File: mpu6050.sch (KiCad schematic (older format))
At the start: 5 parts, among them U2 MPU6050

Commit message: added lots of stuff
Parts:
- added C29: 4.7u, Capacitors_SMD:C_0603, symbol C
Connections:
- net GND: now also C29.2
- net VCC: no longer C16.1, U2.13 (VDD)
- new net VCC_SEN: C16.1, C29.1, U2.13 (VDD)
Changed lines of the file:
@@
 EESchema Schematic File Version 2
+LIBS:stm32f4_lqfp64_mpu6050-rescue
 LIBS:power
 LIBS:device
@@
 LIBS:minimal
 LIBS:alis_parts
+LIBS:sensors
+LIBS:stm32
 LIBS:stm32f4_lqfp64_mpu6050-cache
 EELAYER 25 0
@@
 $Descr A4 11693 8268
 encoding utf-8
-Sheet 5 7
+Sheet 5 10
 Title ""
 Date ""
@@
 	5050 3650 5050 4450
 Wire Wire Line
-	5250 2500 5250 4150
-Wire Wire Line
 	5800 4050 4900 4050
 Wire Wire Line
@@
 	4700 3450 4700 4450
 Connection ~ 5250 4450
-Connection ~ 5250 3750
 Connection ~ 5450 4450
 Wire Wire Line
-	4700 4450 5450 4450
-Connection ~ 5250 3150
+	4400 4450 5450 4450
 Wire Wire Line
 	4700 3150 5800 3150
 Wire Wire Line
-	5800 3750 5250 3750
+	4400 3750 5800 3750
 Connection ~ 5450 3850
-Wire Wire Line
-	5800 3850 5450 3850
 Wire Wire Line
 	5450 2750 5450 4500
@@
 $EndComp
 $Comp
-L GND #PWR22
+L GND #PWR30
 U 1 1 569B8F29
 P 5450 4500
-F 0 "#PWR22" H 5450 4250 50  0001 C CNN
+F 0 "#PWR30" H 5450 4250 50  0001 C CNN
 F 1 "GND" H 5458 4326 50  0000 C CNN
 F 2 "" H 5450 4500 50  0000 C CNN
@@
 	1    0    0    -1
 $EndComp
-Text GLabel 5250 2500 0    60   Input ~ 0
+Text GLabel 4700 3150 0    60   Input ~ 0
 VCC
 Text GLabel 5800 4150 0    60   Input ~ 0
@@
 	1    0    0    -1
 $EndComp
+$Comp
+L C C29
+U 1 1 569B8FE4
+P 4400 4000
+F 0 "C29" H 4515 4046 50  0000 L CNN
+F 1 "4.7u" H 4515 3954 50  0000 L CNN
+F 2 "Capacitors_SMD:C_0603" H 4438 3850 50  0001 C CNN
+F 3 "" H 4400 4000 50  0000 C CNN
+	1    4400 4000
+	1    0    0    -1
+$EndComp
+Wire Wire Line
+	4400 4150 4400 4450
+Connection ~ 4700 4450
+Wire Wire Line
+	5800 3850 5450 3850
+Wire Wire Line
+	4400 3750 4400 3850
+Text GLabel 4400 3750 0    60   Input ~ 0
+VCC_SEN
+Wire Wire Line
+	5250 4150 5250 3750
+Connection ~ 5250 3750
 $EndSCHEMATC

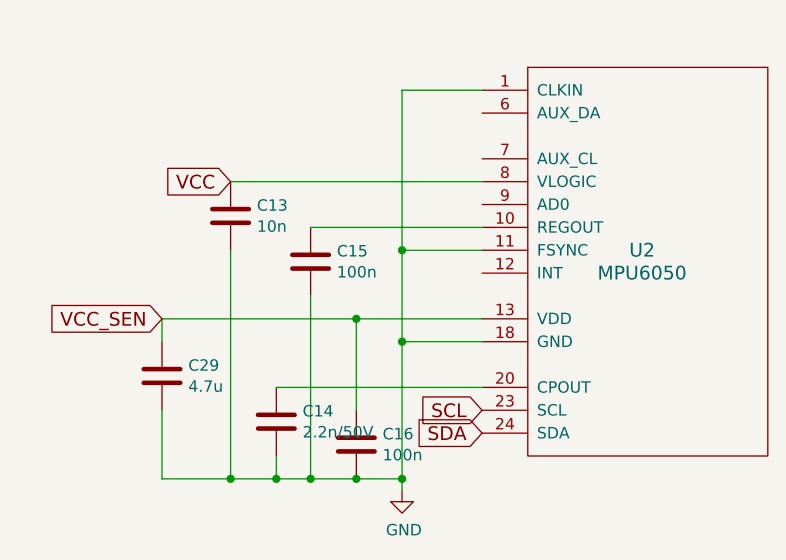
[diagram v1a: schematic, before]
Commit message: added IMU int and USB sense in schematic
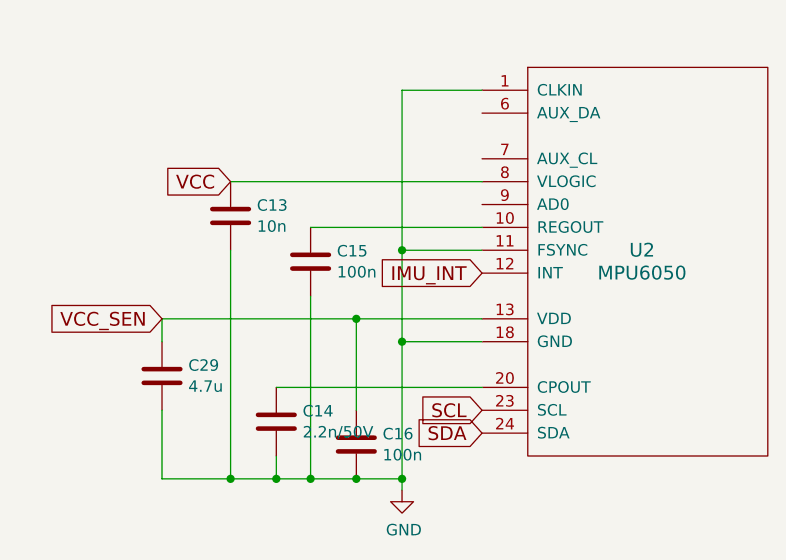
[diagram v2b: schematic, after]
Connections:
- net IMU_INT: now reaches U2.12 (INT)
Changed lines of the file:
@@
 	5250 4150 5250 3750
 Connection ~ 5250 3750
+Text GLabel 5800 3550 0    60   Input ~ 0
+IMU_INT
 $EndSCHEMATC

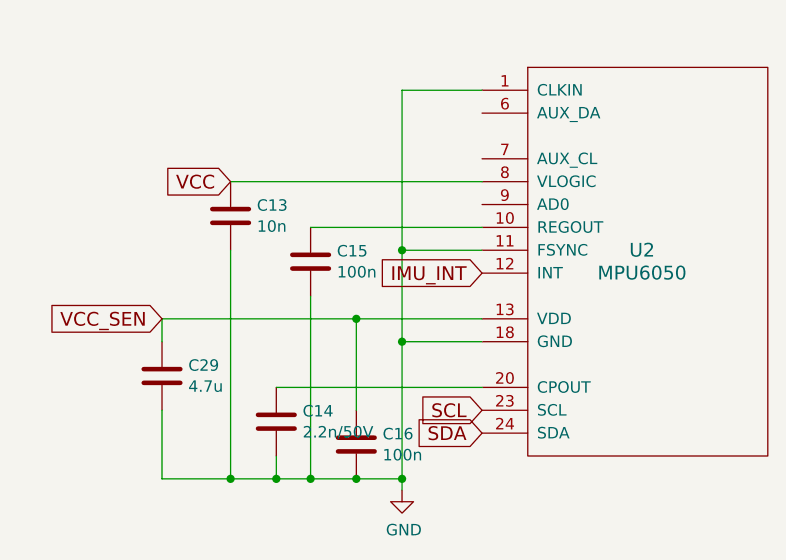
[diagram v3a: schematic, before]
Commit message: changed some netnames
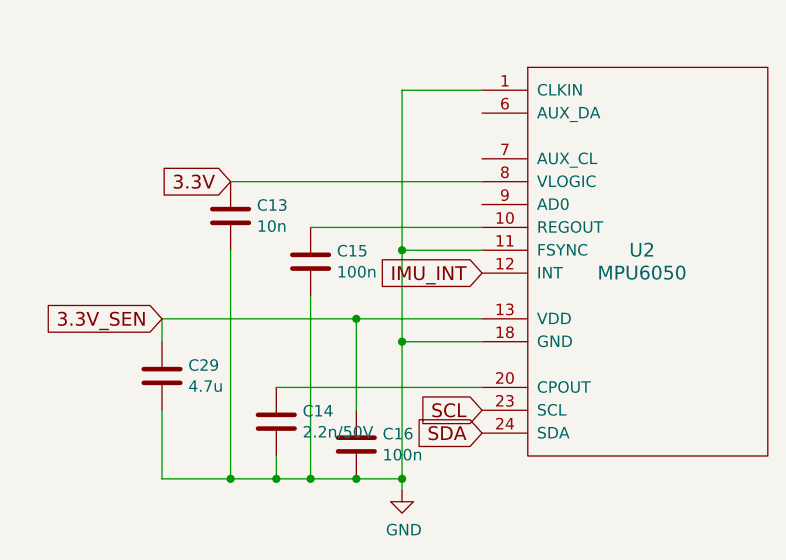
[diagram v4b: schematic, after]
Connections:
- net VCC renamed 3.3V
- net VCC_SEN renamed 3.3V_SEN
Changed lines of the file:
@@
 $EndComp
 $Comp
-L GND #PWR30
+L GND #PWR024
 U 1 1 569B8F29
 P 5450 4500
-F 0 "#PWR30" H 5450 4250 50  0001 C CNN
+F 0 "#PWR024" H 5450 4250 50  0001 C CNN
 F 1 "GND" H 5458 4326 50  0000 C CNN
 F 2 "" H 5450 4500 50  0000 C CNN
@@
 $EndComp
 Text GLabel 4700 3150 0    60   Input ~ 0
-VCC
+3.3V
 Text GLabel 5800 4150 0    60   Input ~ 0
 SCL
@@
 	4400 3750 4400 3850
 Text GLabel 4400 3750 0    60   Input ~ 0
-VCC_SEN
+3.3V_SEN
 Wire Wire Line
 	5250 4150 5250 3750

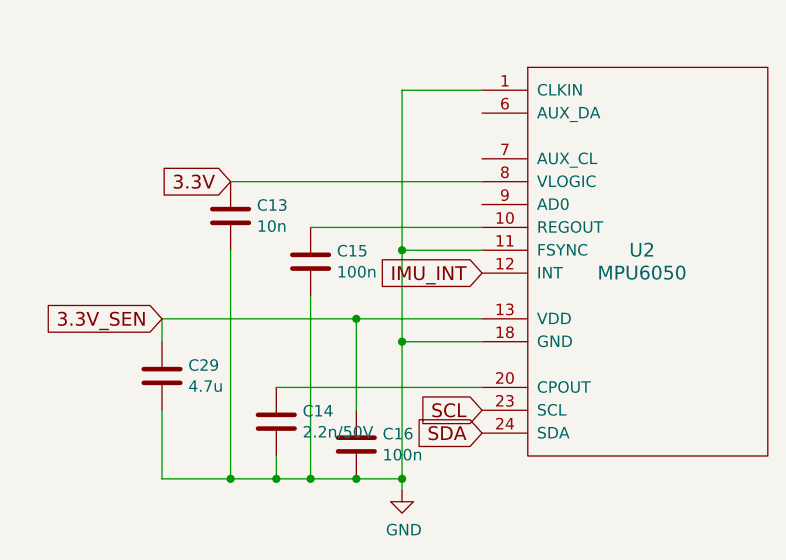
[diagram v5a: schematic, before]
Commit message: power traces routed
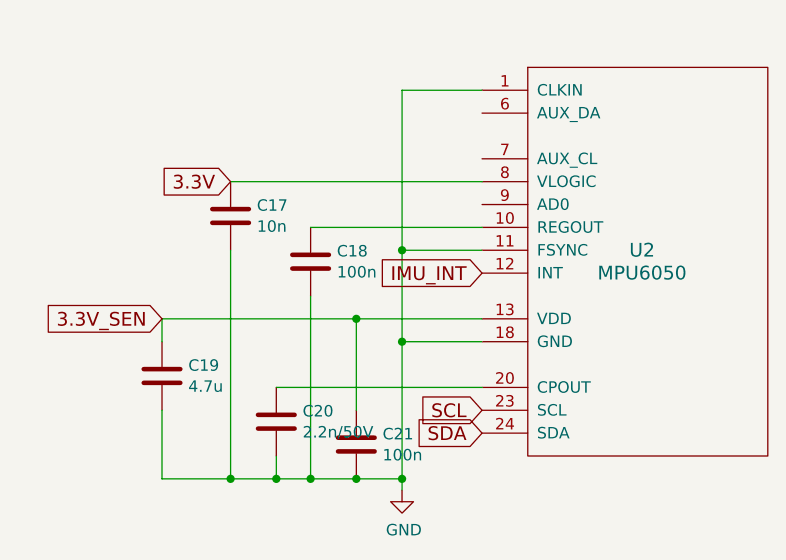
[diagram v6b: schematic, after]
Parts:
- C17: renamed from C13; footprint Capacitors_SMD:C_0402 -> Capacitors_SMD:C_0603
- C18: renamed from C15; footprint Capacitors_SMD:C_0402 -> Capacitors_SMD:C_0603
- C21: renamed from C16; footprint Capacitors_SMD:C_0402 -> Capacitors_SMD:C_0603
- renumbered C29 to C19, C14 to C20
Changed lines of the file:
@@
 $Descr A4 11693 8268
 encoding utf-8
-Sheet 5 7
+Sheet 5 8
 Title ""
 Date ""
@@
 	5800 2750 5450 2750
 $Comp
-L C C15
+L C C18
 U 1 1 569B8F0D
 P 5050 3500
-F 0 "C15" H 5165 3546 50  0000 L CNN
+F 0 "C18" H 5165 3546 50  0000 L CNN
 F 1 "100n" H 5165 3454 50  0000 L CNN
-F 2 "Capacitors_SMD:C_0402" H 5088 3350 50  0001 C CNN
+F 2 "Capacitors_SMD:C_0603" H 5088 3350 50  0001 C CNN
 F 3 "" H 5050 3500 50  0000 C CNN
 	1    5050 3500
@@
 $EndComp
 $Comp
-L C C13
+L C C17
 U 1 1 569B8F14
 P 4700 3300
-F 0 "C13" H 4815 3346 50  0000 L CNN
+F 0 "C17" H 4815 3346 50  0000 L CNN
 F 1 "10n" H 4815 3254 50  0000 L CNN
-F 2 "Capacitors_SMD:C_0402" H 4738 3150 50  0001 C CNN
+F 2 "Capacitors_SMD:C_0603" H 4738 3150 50  0001 C CNN
 F 3 "" H 4700 3300 50  0000 C CNN
 	1    4700 3300
@@
 $EndComp
 $Comp
-L C C16
+L C C21
 U 1 1 569B8F1B
 P 5250 4300
-F 0 "C16" H 5365 4346 50  0000 L CNN
+F 0 "C21" H 5365 4346 50  0000 L CNN
 F 1 "100n" H 5365 4254 50  0000 L CNN
-F 2 "Capacitors_SMD:C_0402" H 5288 4150 50  0001 C CNN
+F 2 "Capacitors_SMD:C_0603" H 5288 4150 50  0001 C CNN
 F 3 "" H 5250 4300 50  0000 C CNN
 	1    5250 4300
@@
 $EndComp
 $Comp
-L C C14
+L C C20
 U 1 1 569B8F22
 P 4900 4200
-F 0 "C14" H 5015 4246 50  0000 L CNN
+F 0 "C20" H 5015 4246 50  0000 L CNN
 F 1 "2.2n/50V" H 5015 4154 50  0000 L CNN
 F 2 "Capacitors_SMD:C_0603" H 4938 4050 50  0001 C CNN
@@
 $EndComp
 $Comp
-L GND #PWR028
+L GND #PWR018
 U 1 1 569B8F29
 P 5450 4500
-F 0 "#PWR028" H 5450 4250 50  0001 C CNN
+F 0 "#PWR018" H 5450 4250 50  0001 C CNN
 F 1 "GND" H 5458 4326 50  0000 C CNN
 F 2 "" H 5450 4500 50  0000 C CNN
@@
 $EndComp
 $Comp
-L C C29
+L C C19
 U 1 1 569B8FE4
 P 4400 4000
-F 0 "C29" H 4515 4046 50  0000 L CNN
+F 0 "C19" H 4515 4046 50  0000 L CNN
 F 1 "4.7u" H 4515 3954 50  0000 L CNN
 F 2 "Capacitors_SMD:C_0603" H 4438 3850 50  0001 C CNN

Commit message: added I2C pullups and pulled MPU6050 AD0 to GND (DOH)
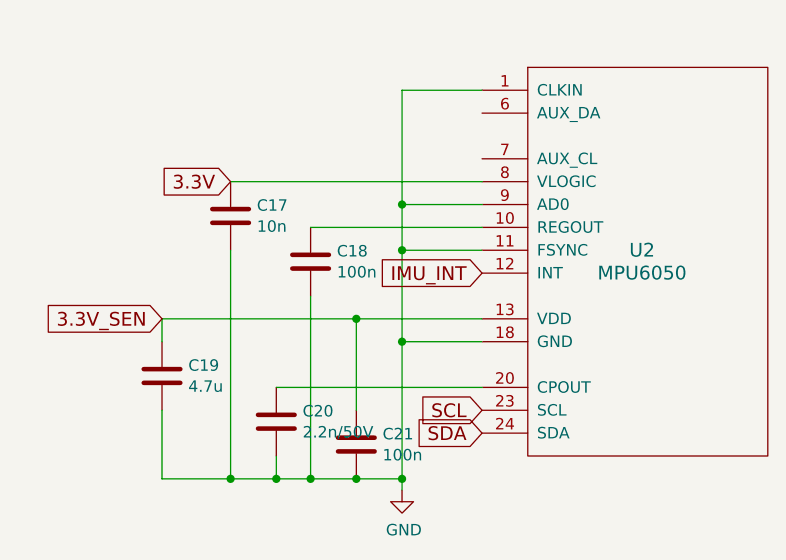
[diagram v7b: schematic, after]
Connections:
- net GND: now also U2.9 (AD0)
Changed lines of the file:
@@
 $Descr A4 11693 8268
 encoding utf-8
-Sheet 5 8
+Sheet 4 8
 Title ""
 Date ""
@@
 Text GLabel 5800 3550 0    60   Input ~ 0
 IMU_INT
+Wire Wire Line
+	5800 3250 5450 3250
+Connection ~ 5450 3250
 $EndSCHEMATC

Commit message: added lt6206 and replaced lm1881 with lmh1980. routing unfinished.
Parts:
- C19: footprint Capacitors_SMD:C_0603 -> Capacitors_SMD:C_0805
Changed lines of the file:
@@
 F 0 "C19" H 4515 4046 50  0000 L CNN
 F 1 "4.7u" H 4515 3954 50  0000 L CNN
-F 2 "Capacitors_SMD:C_0603" H 4438 3850 50  0001 C CNN
+F 2 "Capacitors_SMD:C_0805" H 4438 3850 50  0001 C CNN
 F 3 "" H 4400 4000 50  0000 C CNN
 	1    4400 4000
